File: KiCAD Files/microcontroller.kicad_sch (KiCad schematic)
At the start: 30 parts, among them IC5 AZ1117IH-3.3TRG1, J3 TSW-103-14-S-D, J4 TSW-103-14-S-D, U1 STM32H7A3RGTx, Y1 ABM8G-48.000MHZ-18-D2Y-T

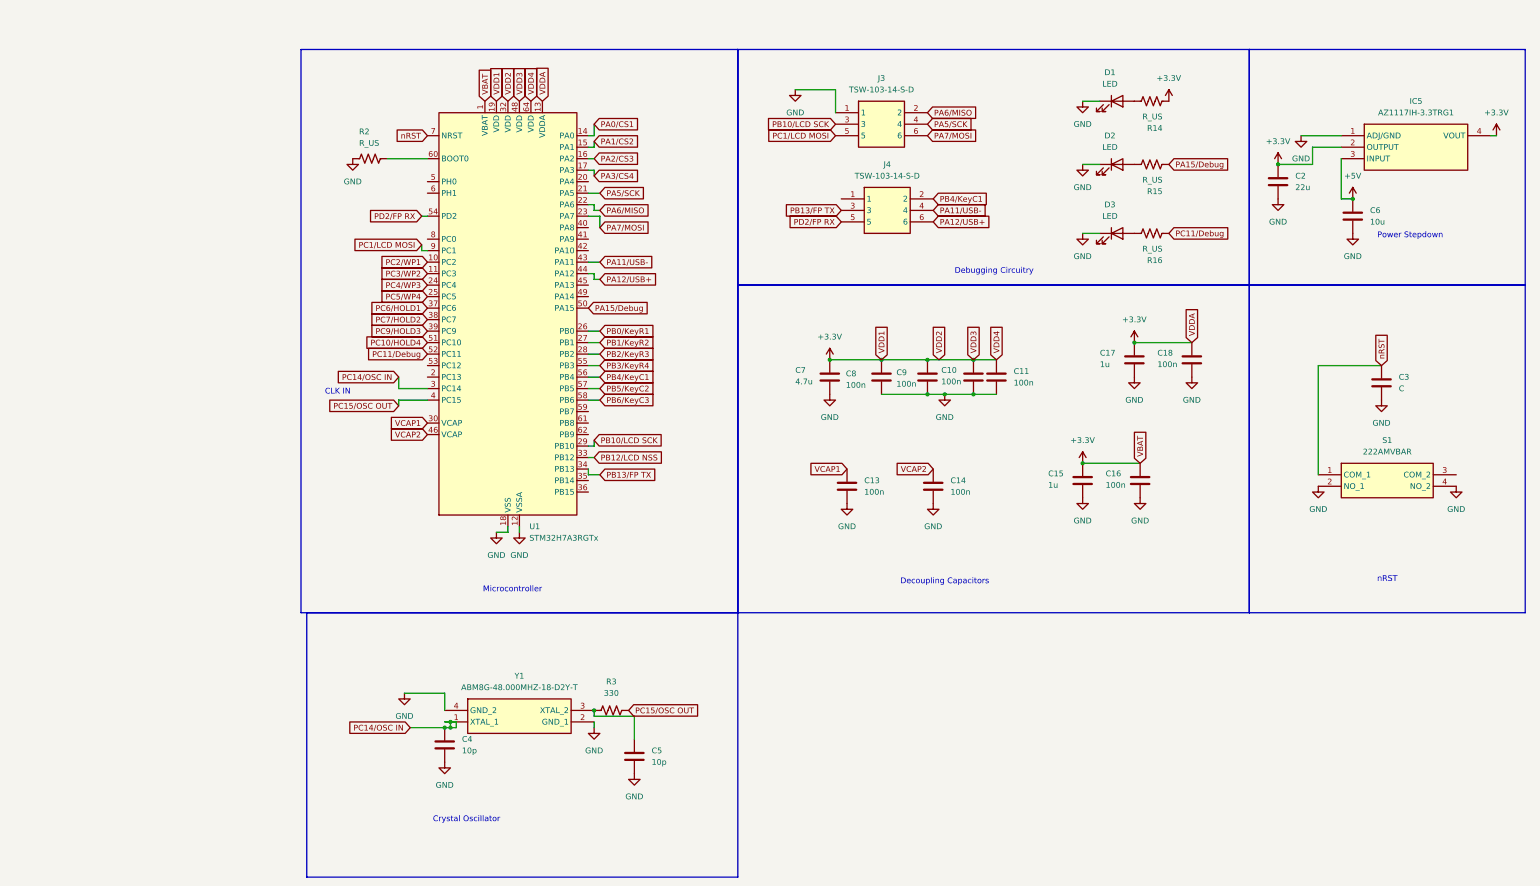
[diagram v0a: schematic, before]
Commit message: tweaked schematic to pass erc
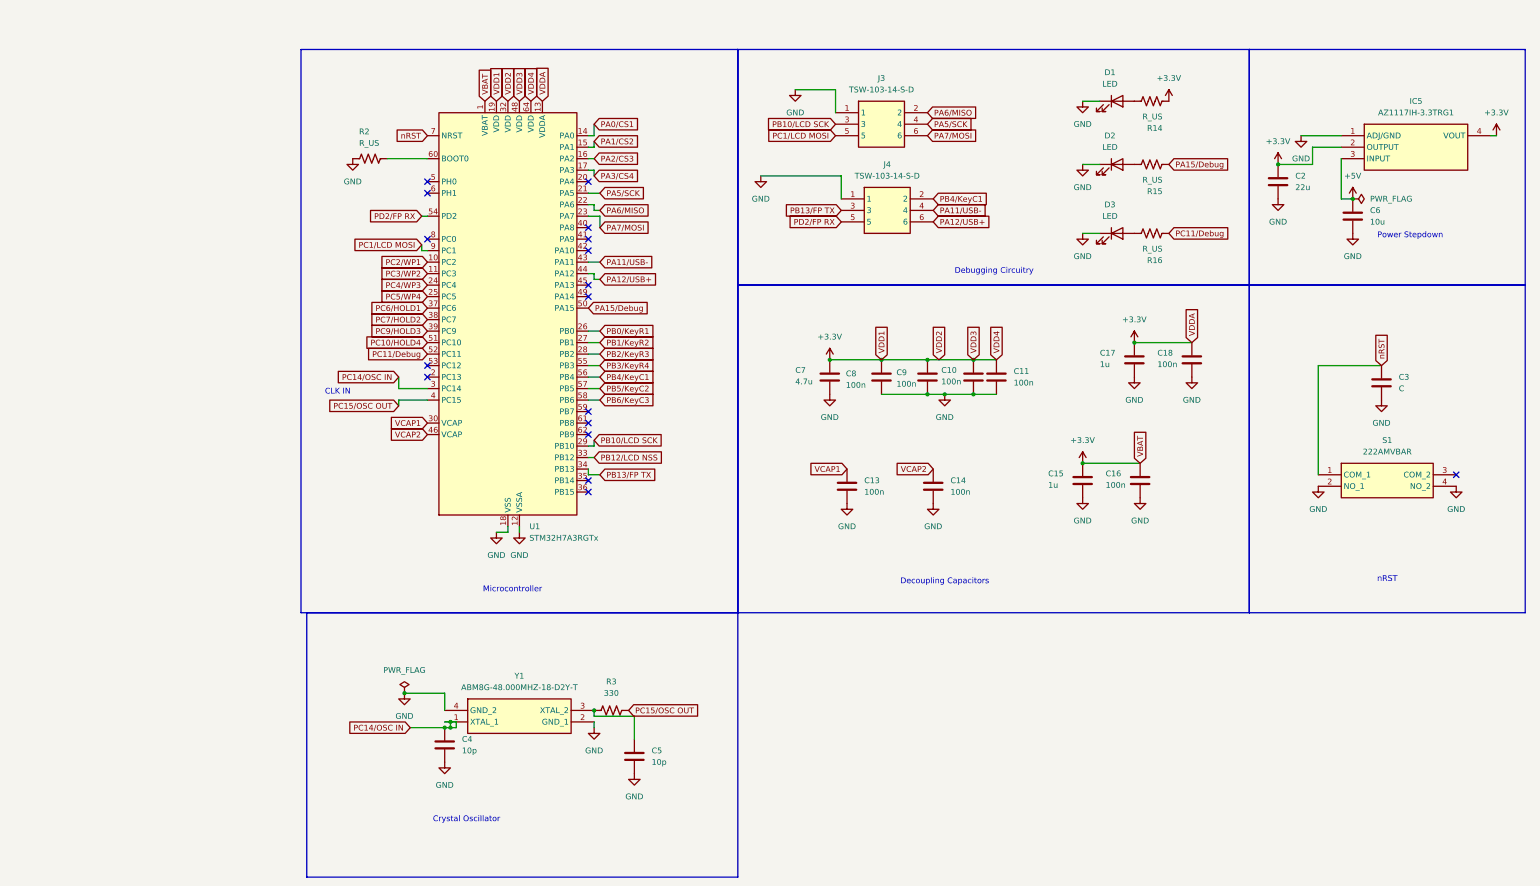
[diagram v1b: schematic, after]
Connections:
- net GND: now also J4.1
- no-connect marks 0 -> 17

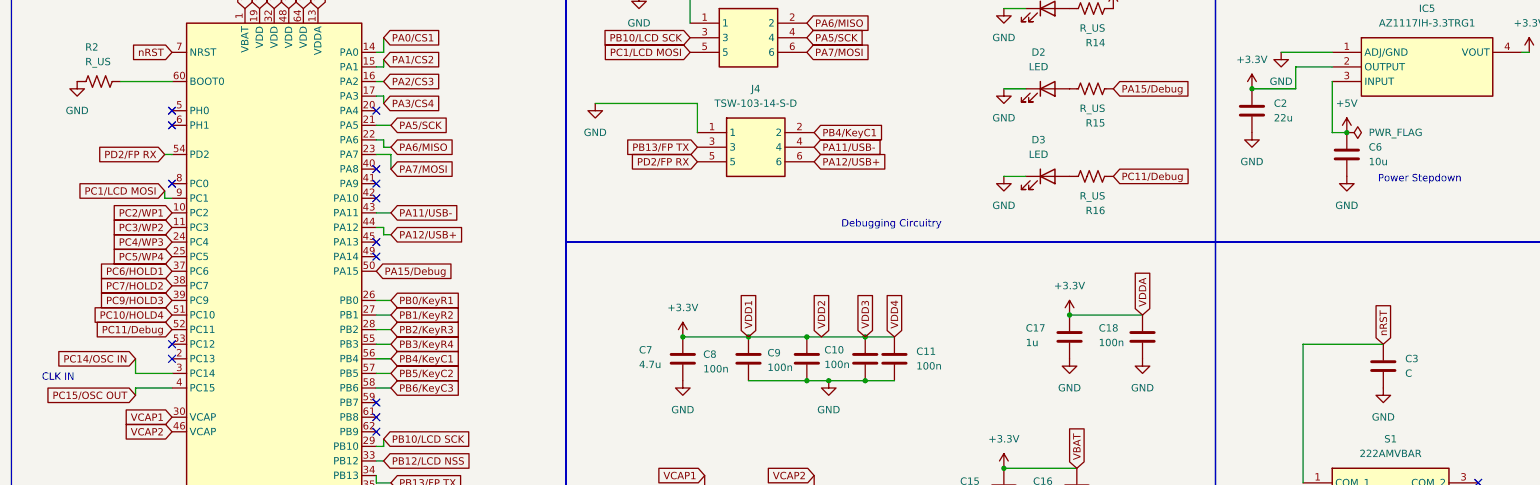
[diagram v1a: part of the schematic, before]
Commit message: added additional connector
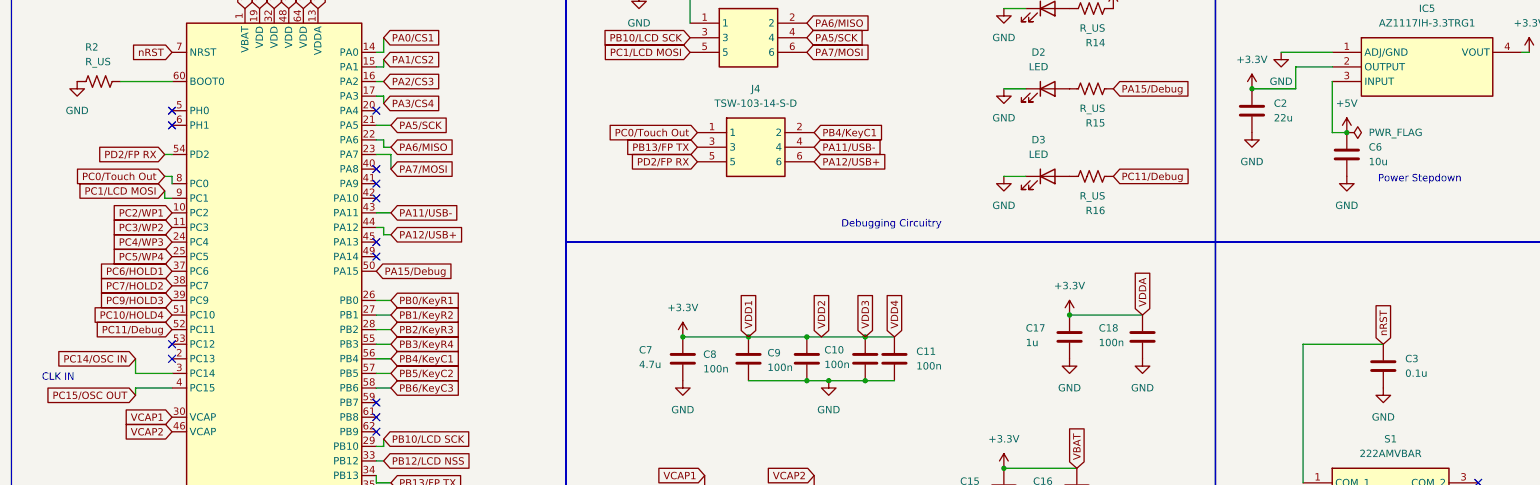
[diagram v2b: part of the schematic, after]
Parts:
- C3: value C -> 0.1u
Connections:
- net GND: no longer J4.1
- net PC0/Touch Out: now reaches U1.8 (PC0)
- net PC0/Touch Out: now also J4.1
- no-connect marks 17 -> 16
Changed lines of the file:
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@@
 		(at 40.64 41.91)
 	)
-	(no_connect
-		(at 40.64 54.61)
-	)
 	(wire
 		(pts
@@
 	(wire
 		(pts
+			(xy 39.37 53.34) (xy 40.64 53.34)
+		)
+		(stroke
+			(width 0)
+			(type default)
+		)
+	)
+	(wire
+		(pts
 			(xy 77.47 31.75) (xy 77.47 29.21)
 		)
@@
 	(wire
 		(pts
-			(xy 132.08 45.72) (xy 132.08 40.64)
-		)
-		(stroke
-			(width 0)
-			(type default)
-		)
-	)
-	(wire
-		(pts
 			(xy 76.2 80.01) (xy 78.74 80.01)
 		)
@@
 	(wire
 		(pts
-			(xy 132.08 40.64) (xy 114.3 40.64)
+			(xy 77.47 39.37) (xy 77.47 40.64)
 		)
 		(stroke
@@
 	(wire
 		(pts
-			(xy 77.47 39.37) (xy 77.47 40.64)
+			(xy 40.64 57.15) (xy 39.37 57.15)
 		)
 		(stroke
@@
 	(wire
 		(pts
-			(xy 40.64 57.15) (xy 39.37 57.15)
+			(xy 77.47 99.06) (xy 77.47 100.33)
 		)
 		(stroke
@@
 	(wire
 		(pts
-			(xy 77.47 99.06) (xy 77.47 100.33)
+			(xy 45.72 161.29) (xy 46.99 161.29)
 		)
 		(stroke
@@
 	(wire
 		(pts
-			(xy 45.72 161.29) (xy 46.99 161.29)
+			(xy 86.36 165.1) (xy 86.36 160.02)
 		)
 		(stroke
@@
 	(wire
 		(pts
-			(xy 86.36 165.1) (xy 86.36 160.02)
+			(xy 77.47 46.99) (xy 76.2 46.99)
 		)
 		(stroke
@@
 	(wire
 		(pts
-			(xy 77.47 46.99) (xy 76.2 46.99)
+			(xy 40.64 53.34) (xy 40.64 54.61)
 		)
 		(stroke
@@
 		)
 	)
+	(global_label "PC0{slash}Touch Out"
+		(shape input)
+		(at 132.08 45.72 180)
+		(fields_autoplaced yes)
+		(effects
+			(font
+				(size 1.27 1.27)
+				(color 0 0 0 1)
+			)
+			(justify right)
+		)
+		(property "Intersheetrefs" "${INTERSHEET_REFS}"
+			(at 114.3388 45.72 0)
+			(effects
+				(font
+					(size 1.27 1.27)
+				)
+				(justify right)
+				(hide yes)
+			)
+		)
+	)
 	(global_label "PB10{slash}LCD SCK"
 		(shape input)
@@
 		)
 	)
+	(global_label "PC0{slash}Touch Out"
+		(shape input)
+		(at 39.37 53.34 180)
+		(fields_autoplaced yes)
+		(effects
+			(font
+				(size 1.27 1.27)
+				(color 0 0 0 1)
+			)
+			(justify right)
+		)
+		(property "Intersheetrefs" "${INTERSHEET_REFS}"
+			(at 21.6288 53.34 0)
+			(effects
+				(font
+					(size 1.27 1.27)
+				)
+				(justify right)
+				(hide yes)
+			)
+		)
+	)
 	(global_label "PD2{slash}FP RX"
 		(shape input)
@@
 			)
 		)
-		(property "Value" "C"
+		(property "Value" "0.1u"
 			(at 255.27 87.6299 0)
 			(effects
@@
 					(unit 1)
 				)
-			)
-		)
-	)
-	(symbol
-		(lib_id "CustomSymbols:GND")
-		(at 114.3 40.64 0)
-		(unit 1)
-		(exclude_from_sim no)
-		(in_bom yes)
-		(on_board yes)
-		(dnp no)
-		(fields_autoplaced yes)
-		(property "Reference" "#PWR056"
-			(at 114.3 46.99 0)
-			(effects
-				(font
-					(size 1.27 1.27)
-				)
-				(hide yes)
-			)
-		)
-		(property "Value" "GND"
-			(at 114.3 45.72 0)
-			(effects
-				(font
-					(size 1.27 1.27)
-				)
-			)
-		)
-		(property "Footprint" ""
-			(at 114.3 40.64 0)
-			(effects
-				(font
-					(size 1.27 1.27)
-				)
-				(hide yes)
-			)
-		)
-		(property "Datasheet" ""
-			(at 114.3 40.64 0)
-			(effects
-				(font
-					(size 1.27 1.27)
-				)
-				(hide yes)
-			)
-		)
-		(property "Description" "Power symbol creates a global label with name \"GND\" , ground"
-			(at 114.3 40.64 0)
-			(effects
-				(font
-					(size 1.27 1.27)
-				)
-				(hide yes)
-			)
-		)
-		(pin "1"
-		)
-		(instances
-			(project ""
-				(path "/b633f67e-3a02-4f0f-b079-02d1853b4f15/e8b68c2d-7a8c-4c60-b0ed-d46a3d1cc27a"
-					(reference "#PWR056")
-					(unit 1)
-				)

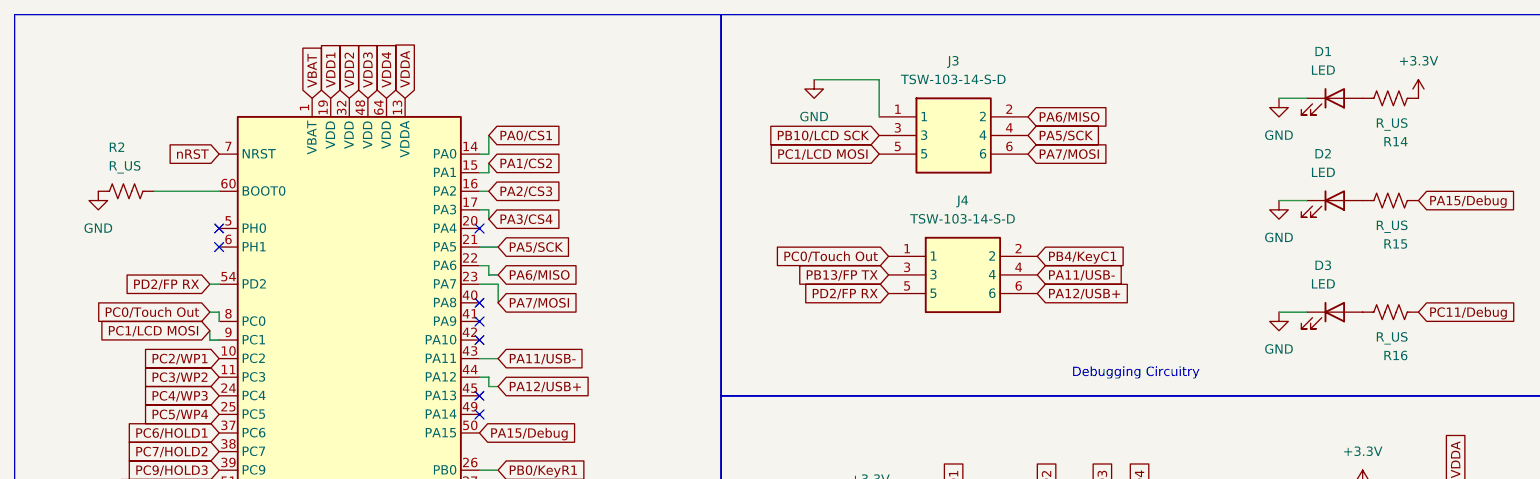
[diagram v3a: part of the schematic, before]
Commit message: finalized schematic
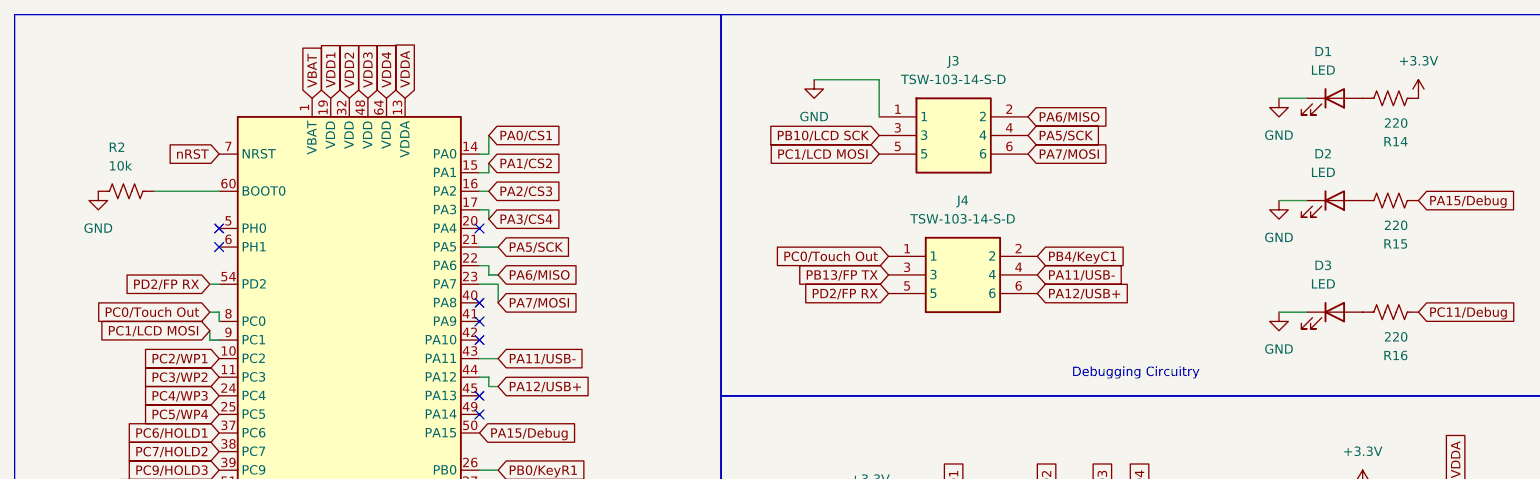
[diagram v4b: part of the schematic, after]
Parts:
- R14, R15, R16: value R_US -> 220
- R2: value R_US -> 10k
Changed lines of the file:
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@@
 			)
 		)
-		(property "Value" "R_US"
+		(property "Value" "220"
 			(at 203.073 56.769 90)
 			(effects
@@
 			)
 		)
-		(property "Value" "R_US"
+		(property "Value" "220"
 			(at 203.073 27.559 90)
 			(effects
@@
 			)
 		)
-		(property "Value" "R_US"
+		(property "Value" "10k"
 			(at 25.527 33.401 90)
 			(effects
@@
 			)
 		)
-		(property "Value" "R_US"
+		(property "Value" "220"
 			(at 203.073 41.529 90)
 			(effects
